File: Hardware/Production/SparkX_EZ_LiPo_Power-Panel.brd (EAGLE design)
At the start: 187.2 x 136.7 mm, 1656 parts, among them J10 AVR_SPI_PROG_3X2TESTPOINTS, J12 AVR_SPI_PROG_3X2TESTPOINTS, J14 AVR_SPI_PROG_3X2TESTPOINTS, J16 AVR_SPI_PROG_3X2TESTPOINTS, J18 AVR_SPI_PROG_3X2TESTPOINTS, J20 AVR_SPI_PROG_3X2TESTPOINTS, J22 AVR_SPI_PROG_3X2TESTPOINTS, J24 AVR_SPI_PROG_3X2TESTPOINTS, J26 AVR_SPI_PROG_3X2TESTPOINTS, J28 AVR_SPI_PROG_3X2TESTPOINTS, J3 AVR_SPI_PROG_3X2TESTPOINTS, J30 AVR_SPI_PROG_3X2TESTPOINTS, J32 AVR_SPI_PROG_3X2TESTPOINTS, J34 AVR_SPI_PROG_3X2TESTPOINTS, J36 AVR_SPI_PROG_3X2TESTPOINTS, J38 AVR_SPI_PROG_3X2TESTPOINTS, J4 AVR_SPI_PROG_3X2TESTPOINTS, J40 AVR_SPI_PROG_3X2TESTPOINTS, J42 AVR_SPI_PROG_3X2TESTPOINTS, J44 AVR_SPI_PROG_3X2TESTPOINTS, J46 AVR_SPI_PROG_3X2TESTPOINTS, J48 AVR_SPI_PROG_3X2TESTPOINTS, J50 AVR_SPI_PROG_3X2TESTPOINTS, J52 AVR_SPI_PROG_3X2TESTPOINTS, J54 AVR_SPI_PROG_3X2TESTPOINTS, J56 AVR_SPI_PROG_3X2TESTPOINTS, J58 AVR_SPI_PROG_3X2TESTPOINTS, J6 AVR_SPI_PROG_3X2TESTPOINTS, J60 AVR_SPI_PROG_3X2TESTPOINTS, J8 AVR_SPI_PROG_3X2TESTPOINTS, Q1 3.1A/30V/105mΩ, Q10 3.1A/30V/105mΩ, Q11 3.1A/30V/105mΩ, Q12 3.1A/30V/105mΩ, Q13 3.1A/30V/105mΩ, Q14 3.1A/30V/105mΩ, Q15 3.1A/30V/105mΩ, Q16 3.1A/30V/105mΩ, Q17 3.1A/30V/105mΩ, Q18 3.1A/30V/105mΩ, Q19 3.1A/30V/105mΩ, Q2 3.1A/30V/105mΩ, Q20 3.1A/30V/105mΩ, Q21 3.1A/30V/105mΩ, Q22 3.1A/30V/105mΩ, Q23 3.1A/30V/105mΩ, Q24 3.1A/30V/105mΩ, Q25 3.1A/30V/105mΩ, Q26 3.1A/30V/105mΩ, Q27 3.1A/30V/105mΩ, Q28 3.1A/30V/105mΩ, Q29 3.1A/30V/105mΩ, Q3 3.1A/30V/105mΩ, Q30 3.1A/30V/105mΩ, Q4 3.1A/30V/105mΩ, Q5 3.1A/30V/105mΩ, Q6 3.1A/30V/105mΩ, Q7 3.1A/30V/105mΩ, Q8 3.1A/30V/105mΩ, Q9 3.1A/30V/105mΩ, U1 STLQ015-3.3V, U10 STLQ015-3.3V, U100 STLQ015-3.3V, U101 MCP73831, U102 3.3V, U103 MAX17048, U104 ATTINY841-ARDUINO_QFN20M1, U105 STLQ015-3.3V, U106 MCP73831, U107 3.3V, U108 MAX17048, U109 ATTINY841-ARDUINO_QFN20M1, U11 MCP73831, U110 STLQ015-3.3V, U111 MCP73831, U112 3.3V, U113 MAX17048, U114 ATTINY841-ARDUINO_QFN20M1, U115 STLQ015-3.3V, U116 MCP73831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

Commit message: Final tweaks
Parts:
- added U$481, U$482, U$498, U$499: (no value), output:EZ_POWER_LIPO0
- added U$483, U$500: (no value), output:#BATT##0
- added U$484, U$501: (no value), output:#VIN#0
- added U$485, U$502: (no value), output:#3V3_EN#0
- added U$486, U$503: (no value), output:#PROC_PWR#0
- added U$487, U$504: (no value), output:#AT_VCC#0
- added U$488, U$505: (no value), output:#FG_SDA#0
- added U$489, U$506: (no value), output:CHG0
- added U$490, U$507: (no value), output:#RXD0#0
- added U$491, U$508: (no value), output:#TXD0#0
- added U$492, U$509: (no value), output:5#5V0
- added U$493, U$510: (no value), output:MAX0
- added U$494, U$496: SPARKX-LOGO3, SparkX:SPARKX-SMALL
- added U$495: (no value), output:#OUT#0
- added U$497: (no value), output:#IN#0
- U$100, U$372: device output:#IN#0 -> output:#TXD0#0
- U$101, U$118, U$373, U$390: device output:EZ_POWER_LIPO0 -> output:5#5V0
- U$102, U$357, U$374, U$85: device output:EZ_POWER_LIPO0 -> output:MAX0
- U$103, U$343, U$375, U$71: value (none) -> SPARKX-LOGO3; device output:#BATT##0 -> SparkX:SPARKX-SMALL
- U$104, U$376: device output:#VIN#0 -> output:#OUT#0
- U$105, U$137, U$377, U$409: value (none) -> SPARKX-LOGO3; device output:#3V3_EN#0 -> SparkX:SPARKX-SMALL
- U$106, U$378: device output:#PROC_PWR#0 -> output:#IN#0
- U$107, U$363, U$379, U$91: device output:#AT_VCC#0 -> output:EZ_POWER_LIPO0
- U$108, U$124, U$380, U$396: device output:#FG_SDA#0 -> output:EZ_POWER_LIPO0
- U$109, U$381: device output:CHG0 -> output:#BATT##0
- U$11, U$238: device output:5#5V_MAX0 -> output:MAX0
- U$110, U$382: device output:5#5V_MAX0 -> output:#VIN#0
- U$111, U$383: device output:#RXD0#0 -> output:#3V3_EN#0
- U$112, U$384: device output:#TXD0#0 -> output:#PROC_PWR#0
- U$113, U$147, U$385, U$419: value SPARKX-LOGO3 -> (none); device SparkX:SPARKX-SMALL -> output:#AT_VCC#0
- U$114, U$386: device output:#OUT#0 -> output:#FG_SDA#0
- U$115, U$353, U$387, U$81: value SPARKX-LOGO3 -> (none); device SparkX:SPARKX-SMALL -> output:CHG0
- U$116, U$388: device output:#IN#0 -> output:#RXD0#0
- U$117, U$134, U$389, U$406: device output:EZ_POWER_LIPO0 -> output:#TXD0#0
- U$119, U$391: device output:#BATT##0 -> output:MAX0
- U$120, U$360, U$392, U$88: value (none) -> SPARKX-LOGO3; device output:#VIN#0 -> SparkX:SPARKX-SMALL
- U$121, U$393: device output:#3V3_EN#0 -> output:#OUT#0
- U$122, U$154, U$394, U$426: value (none) -> SPARKX-LOGO3; device output:#PROC_PWR#0 -> SparkX:SPARKX-SMALL
- U$123, U$395: device output:#AT_VCC#0 -> output:#IN#0
- U$125, U$141, U$397, U$413: device output:CHG0 -> output:EZ_POWER_LIPO0
- U$126, U$398: device output:5#5V_MAX0 -> output:#BATT##0
- U$127, U$399: device output:#RXD0#0 -> output:#VIN#0
- U$128, U$400: device output:#TXD0#0 -> output:#3V3_EN#0
- U$129, U$163, U$401, U$435: value SPARKX-LOGO3 -> (none); device SparkX:SPARKX-SMALL -> output:#PROC_PWR#0
- U$130, U$402: device output:#OUT#0 -> output:#AT_VCC#0
- U$131, U$369, U$403, U$97: value SPARKX-LOGO3 -> (none); device SparkX:SPARKX-SMALL -> output:#FG_SDA#0
- U$132, U$404: device output:#IN#0 -> output:CHG0
- U$133, U$150, U$405, U$422: device output:EZ_POWER_LIPO0 -> output:#RXD0#0
- U$135, U$407: device output:#BATT##0 -> output:5#5V0
- U$136, U$408: device output:#VIN#0 -> output:MAX0
- U$138, U$410: device output:#PROC_PWR#0 -> output:#OUT#0
- U$139, U$171, U$411, U$443: value (none) -> SPARKX-LOGO3; device output:#AT_VCC#0 -> SparkX:SPARKX-SMALL
- U$140, U$412: device output:#FG_SDA#0 -> output:#IN#0
- U$142, U$158, U$414, U$430: device output:5#5V_MAX0 -> output:EZ_POWER_LIPO0
- U$143, U$415: device output:#RXD0#0 -> output:#BATT##0
- U$144, U$416: device output:#TXD0#0 -> output:#VIN#0
- U$145, U$179, U$417, U$451: value SPARKX-LOGO3 -> (none); device SparkX:SPARKX-SMALL -> output:#3V3_EN#0
- U$146, U$418: device output:#OUT#0 -> output:#PROC_PWR#0
- U$148, U$420: device output:#IN#0 -> output:#FG_SDA#0
- U$149, U$166, U$421, U$438: device output:EZ_POWER_LIPO0 -> output:CHG0
- U$151, U$423: device output:#BATT##0 -> output:#TXD0#0
- U$152, U$424: device output:#VIN#0 -> output:5#5V0
- U$153, U$425: device output:#3V3_EN#0 -> output:MAX0
- U$155, U$427: device output:#AT_VCC#0 -> output:#OUT#0
- U$156, U$188, U$428, U$460: value (none) -> SPARKX-LOGO3; device output:#FG_SDA#0 -> SparkX:SPARKX-SMALL
- U$157, U$429: device output:CHG0 -> output:#IN#0
- U$159, U$175, U$431, U$447: device output:#RXD0#0 -> output:EZ_POWER_LIPO0
- U$16, U$305, U$33, U$339, U$67: value SPARKX-LOGO3 -> (none); device SparkX:SPARKX-SMALL -> output:5#5V0
- U$160, U$432: device output:#TXD0#0 -> output:#BATT##0
- U$161, U$195, U$433, U$467: value SPARKX-LOGO3 -> (none); device SparkX:SPARKX-SMALL -> output:#VIN#0
- U$162, U$434: device output:#OUT#0 -> output:#3V3_EN#0
- U$164, U$436: device output:#IN#0 -> output:#AT_VCC#0
- U$165, U$182, U$437, U$454: device output:EZ_POWER_LIPO0 -> output:#FG_SDA#0
- U$167, U$439: device output:#BATT##0 -> output:#RXD0#0
- U$168, U$440: device output:#VIN#0 -> output:#TXD0#0
- U$169, U$441: device output:#3V3_EN#0 -> output:5#5V0
- U$17, U$258, U$290: value (none) -> SPARKX-LOGO3; device output:#OUT#0 -> SparkX:SPARKX-SMALL
- U$170, U$442: device output:#PROC_PWR#0 -> output:MAX0
- U$172, U$444: device output:#FG_SDA#0 -> output:#OUT#0
- U$173, U$205, U$445, U$477: value (none) -> SPARKX-LOGO3; device output:CHG0 -> SparkX:SPARKX-SMALL
- U$174, U$446: device output:5#5V_MAX0 -> output:#IN#0
- U$176, U$192, U$448, U$464: device output:#TXD0#0 -> output:EZ_POWER_LIPO0
- U$177, U$211, U$449: value SPARKX-LOGO3 -> (none); device SparkX:SPARKX-SMALL -> output:#BATT##0
- U$178, U$450: device output:#OUT#0 -> output:#VIN#0
- U$18, U$257, U$291: value SPARKX-LOGO3 -> (none); device SparkX:SPARKX-SMALL -> output:#OUT#0
- U$180, U$452: device output:#IN#0 -> output:#PROC_PWR#0
- U$181, U$198, U$453, U$470: device output:EZ_POWER_LIPO0 -> output:#AT_VCC#0
- U$183, U$455: device output:#BATT##0 -> output:CHG0
- U$184, U$456: device output:#VIN#0 -> output:#RXD0#0
- U$185, U$457: device output:#3V3_EN#0 -> output:#TXD0#0
- U$186, U$458: device output:#PROC_PWR#0 -> output:5#5V0
- U$187, U$459: device output:#AT_VCC#0 -> output:MAX0
- U$189, U$461: device output:CHG0 -> output:#OUT#0
- U$19, U$292, U$324, U$52: value (none) -> SPARKX-LOGO3; device output:#IN#0 -> SparkX:SPARKX-SMALL
- U$190, U$222, U$462: value (none) -> SPARKX-LOGO3; device output:5#5V_MAX0 -> SparkX:SPARKX-SMALL
- U$191, U$463: device output:#RXD0#0 -> output:#IN#0
- U$193, U$209, U$227, U$243, U$465: value SPARKX-LOGO3 -> (none); device SparkX:SPARKX-SMALL -> output:EZ_POWER_LIPO0
- U$194, U$466: device output:#OUT#0 -> output:#BATT##0
- U$196, U$468: device output:#IN#0 -> output:#3V3_EN#0
- U$197, U$214, U$469: device output:EZ_POWER_LIPO0 -> output:#PROC_PWR#0
- U$199, U$471: device output:#BATT##0 -> output:#FG_SDA#0
- U$200, U$472: device output:#VIN#0 -> output:CHG0
- U$201, U$473: device output:#3V3_EN#0 -> output:#RXD0#0
- U$202, U$474: device output:#PROC_PWR#0 -> output:#TXD0#0
- U$203, U$475: device output:#AT_VCC#0 -> output:5#5V0
- U$204, U$476: device output:#FG_SDA#0 -> output:MAX0
- U$206, U$478: device output:5#5V_MAX0 -> output:#OUT#0
- U$207, U$239, U$479: value (none) -> SPARKX-LOGO3; device output:#RXD0#0 -> SparkX:SPARKX-SMALL
- U$208, U$480: device output:#TXD0#0 -> output:#IN#0
- U$21, U$293, U$310, U$38: device output:EZ_POWER_LIPO0 -> output:#IN#0
- U$210, U$226: device output:#OUT#0 -> output:EZ_POWER_LIPO0
- U$212: device output:#IN#0 -> output:#VIN#0
- U$213, U$230: device output:EZ_POWER_LIPO0 -> output:#3V3_EN#0
- U$215: device output:#BATT##0 -> output:#AT_VCC#0
- U$216: device output:#VIN#0 -> output:#FG_SDA#0
- U$217: device output:#3V3_EN#0 -> output:CHG0
- U$218: device output:#PROC_PWR#0 -> output:#RXD0#0
- U$219: device output:#AT_VCC#0 -> output:#TXD0#0
- U$220: device output:#FG_SDA#0 -> output:5#5V0
- U$221: device output:CHG0 -> output:MAX0
- U$223: device output:#RXD0#0 -> output:#OUT#0
- U$224, U$256: value (none) -> SPARKX-LOGO3; device output:#TXD0#0 -> SparkX:SPARKX-SMALL
- U$225, U$259: value SPARKX-LOGO3 -> (none); device SparkX:SPARKX-SMALL -> output:#IN#0
- U$228: device output:#IN#0 -> output:#BATT##0
- U$229, U$246: device output:EZ_POWER_LIPO0 -> output:#VIN#0
- U$23, U$295, U$311, U$39: device output:#BATT##0 -> output:EZ_POWER_LIPO0
- U$231: device output:#BATT##0 -> output:#PROC_PWR#0
- U$232: device output:#VIN#0 -> output:#AT_VCC#0
- U$233: device output:#3V3_EN#0 -> output:#FG_SDA#0
- U$234: device output:#PROC_PWR#0 -> output:CHG0
- U$235: device output:#AT_VCC#0 -> output:#RXD0#0
- U$236: device output:#FG_SDA#0 -> output:#TXD0#0
- U$237: device output:CHG0 -> output:5#5V0
- U$24, U$296: device output:#VIN#0 -> output:#BATT##0
- U$240: device output:#TXD0#0 -> output:#OUT#0
- U$242: device output:#OUT#0 -> output:#IN#0
- U$244, U$260: device output:#IN#0 -> output:EZ_POWER_LIPO0
- U$245, U$262: device output:EZ_POWER_LIPO0 -> output:#BATT##0
- U$247: device output:#BATT##0 -> output:#3V3_EN#0
- U$248: device output:#VIN#0 -> output:#PROC_PWR#0
- U$249: device output:#3V3_EN#0 -> output:#AT_VCC#0
- U$25, U$297: device output:#3V3_EN#0 -> output:#VIN#0
- U$250: device output:#PROC_PWR#0 -> output:#FG_SDA#0
- U$251: device output:#AT_VCC#0 -> output:CHG0
- U$252: device output:#FG_SDA#0 -> output:#RXD0#0
- U$253: device output:CHG0 -> output:#TXD0#0
- U$254: device output:5#5V_MAX0 -> output:5#5V0
- U$255: device output:#RXD0#0 -> output:MAX0
- U$26, U$298: device output:#PROC_PWR#0 -> output:#3V3_EN#0
- U$263: device output:#BATT##0 -> output:#VIN#0
- U$264: device output:#VIN#0 -> output:#3V3_EN#0
- U$265: device output:#3V3_EN#0 -> output:#PROC_PWR#0
- U$266: device output:#PROC_PWR#0 -> output:#AT_VCC#0
- U$267: device output:#AT_VCC#0 -> output:#FG_SDA#0
- U$268: device output:#FG_SDA#0 -> output:CHG0
- U$269: device output:CHG0 -> output:#RXD0#0
- U$27, U$299: device output:#AT_VCC#0 -> output:#PROC_PWR#0
- U$270: device output:5#5V_MAX0 -> output:#TXD0#0
- U$271: device output:#RXD0#0 -> output:5#5V0
- U$272: device output:#TXD0#0 -> output:MAX0
- U$28, U$300: device output:#FG_SDA#0 -> output:#AT_VCC#0
- U$286: device output:5#5V_MAX0 -> output:#RXD0#0
- U$287: device output:#RXD0#0 -> output:#TXD0#0
- U$288: device output:#TXD0#0 -> output:5#5V0
- U$289, U$323, U$51: value SPARKX-LOGO3 -> (none); device SparkX:SPARKX-SMALL -> output:MAX0
- U$29, U$301: device output:CHG0 -> output:#FG_SDA#0
- U$30, U$302: device output:5#5V_MAX0 -> output:CHG0
- U$306, U$34: device output:#OUT#0 -> output:MAX0
- U$308, U$36: device output:#IN#0 -> output:#OUT#0
- U$309, U$326, U$341, U$358, U$37, U$54, U$69, U$86: value (none) -> SPARKX-LOGO3; device output:EZ_POWER_LIPO0 -> SparkX:SPARKX-SMALL
- U$312, U$328, U$40, U$56: device output:#VIN#0 -> output:EZ_POWER_LIPO0
- U$313, U$41: device output:#3V3_EN#0 -> output:#BATT##0
- U$314, U$42: device output:#PROC_PWR#0 -> output:#VIN#0
- U$315, U$43: device output:#AT_VCC#0 -> output:#3V3_EN#0
- U$316, U$44: device output:#FG_SDA#0 -> output:#PROC_PWR#0
- U$317, U$45: device output:CHG0 -> output:#AT_VCC#0
- U$318, U$46: device output:5#5V_MAX0 -> output:#FG_SDA#0
- U$319, U$47: device output:#RXD0#0 -> output:CHG0
- U$320, U$48: device output:#TXD0#0 -> output:#RXD0#0
- U$321, U$355, U$49, U$83: value SPARKX-LOGO3 -> (none); device SparkX:SPARKX-SMALL -> output:#TXD0#0
- U$322, U$50: device output:#OUT#0 -> output:5#5V0
- U$325, U$342, U$53, U$70: device output:EZ_POWER_LIPO0 -> output:#OUT#0
- U$327, U$55: device output:#BATT##0 -> output:#IN#0
- U$329, U$345, U$57, U$73: device output:#3V3_EN#0 -> output:EZ_POWER_LIPO0
- U$330, U$58: device output:#PROC_PWR#0 -> output:#BATT##0
- U$331, U$59: device output:#AT_VCC#0 -> output:#VIN#0
- U$332, U$60: device output:#FG_SDA#0 -> output:#3V3_EN#0
- U$333, U$61: device output:CHG0 -> output:#PROC_PWR#0
- U$334, U$62: device output:5#5V_MAX0 -> output:#AT_VCC#0
- U$335, U$63: device output:#RXD0#0 -> output:#FG_SDA#0
- U$336, U$64: device output:#TXD0#0 -> output:CHG0
- U$337, U$371, U$65, U$99: value SPARKX-LOGO3 -> (none); device SparkX:SPARKX-SMALL -> output:#RXD0#0
- U$338, U$66: device output:#OUT#0 -> output:#TXD0#0
- U$340, U$68: device output:#IN#0 -> output:MAX0
- U$344, U$72: device output:#VIN#0 -> output:#IN#0
- U$346, U$362, U$74, U$90: device output:#PROC_PWR#0 -> output:EZ_POWER_LIPO0
- U$347, U$75: device output:#AT_VCC#0 -> output:#BATT##0
- U$348, U$76: device output:#FG_SDA#0 -> output:#VIN#0
- U$349, U$77: device output:CHG0 -> output:#3V3_EN#0
- U$350, U$78: device output:5#5V_MAX0 -> output:#PROC_PWR#0
- U$351, U$79: device output:#RXD0#0 -> output:#AT_VCC#0
- U$352, U$80: device output:#TXD0#0 -> output:#FG_SDA#0
- U$354, U$82: device output:#OUT#0 -> output:#RXD0#0
- U$356, U$84: device output:#IN#0 -> output:5#5V0
- U$359, U$87: device output:#BATT##0 -> output:#OUT#0
- U$361, U$89: device output:#3V3_EN#0 -> output:#IN#0
- U$364, U$92: device output:#FG_SDA#0 -> output:#BATT##0
- U$365, U$93: device output:CHG0 -> output:#VIN#0
- U$366, U$94: device output:5#5V_MAX0 -> output:#3V3_EN#0
- U$367, U$95: device output:#RXD0#0 -> output:#PROC_PWR#0
- U$368, U$96: device output:#TXD0#0 -> output:#AT_VCC#0
- U$370, U$98: device output:#OUT#0 -> output:CHG0
- moved U$164 164.7 mm to (155.6, 8.64), flipped to the top, turned to 90 degrees
- moved U$333 163.2 mm to (150.7, 44.9), flipped to the bottom, turned to 0 degrees
- moved U$168 160.8 mm to (154.4, 16.5)
- moved U$334 160.2 mm to (155.6, 49.8)
- moved U$328 159.4 mm to (156.1, 67.2), flipped to the top, turned to 90 degrees
- moved U$163 158.4 mm to (150.7, 3.75)
- moved U$335 157.2 mm to (156.1, 69.8)
- moved U$332 156.4 mm to (153.3, 48.8), turned to 0 degrees
- moved U$324 155.8 mm to (147.8, 54.0), flipped to the top, turned to 90 degrees
- moved U$167 155.7 mm to (147.9, 16.5), turned to 90 degrees
- moved U$325 155.2 mm to (151.6, 46.0), turned to 0 degrees
- moved U$327 153.5 mm to (151.6, 75.9)
- moved U$162 152.9 mm to (153.3, 7.62), flipped to the bottom
- moved U$170 151.7 mm to (155.5, 31.0), flipped to the top
- moved U$165 151.5 mm to (156.1, 28.7), flipped to the bottom
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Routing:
- net GND1: track 82.0 -> 96.0 mm
- net GND7: track 82.0 -> 96.0 mm
- net GND6: track 82.0 -> 96.0 mm
- net GND5: track 82.0 -> 96.0 mm
- net GND2: track 82.0 -> 96.0 mm
- net GND3: track 82.0 -> 96.0 mm
- net GND9: track 82.0 -> 96.0 mm
- net GND8: track 82.0 -> 96.0 mm
- net GND4: track 82.0 -> 96.0 mm
- net GND19: track 82.0 -> 96.0 mm
- net GND18: track 82.0 -> 96.0 mm
- net GND: track 82.0 -> 96.0 mm
- net GND29: track 82.0 -> 96.0 mm
- net GND28: track 82.0 -> 96.0 mm
- net GND27: track 82.0 -> 96.0 mm
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
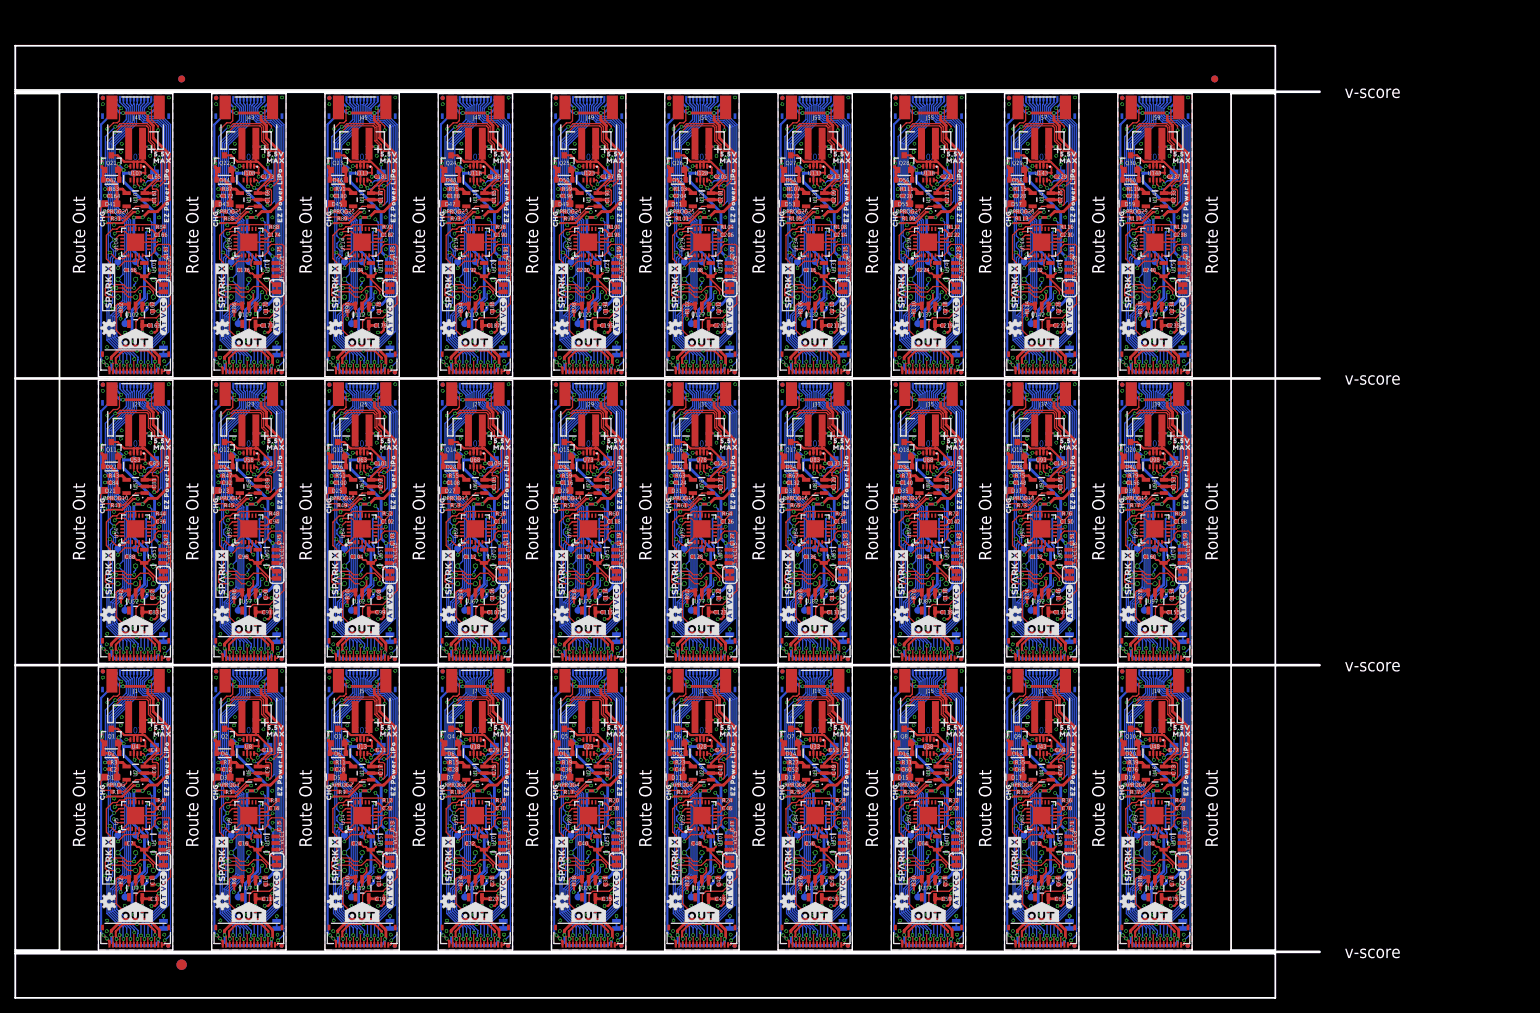
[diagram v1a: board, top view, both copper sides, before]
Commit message: Gapless production panel
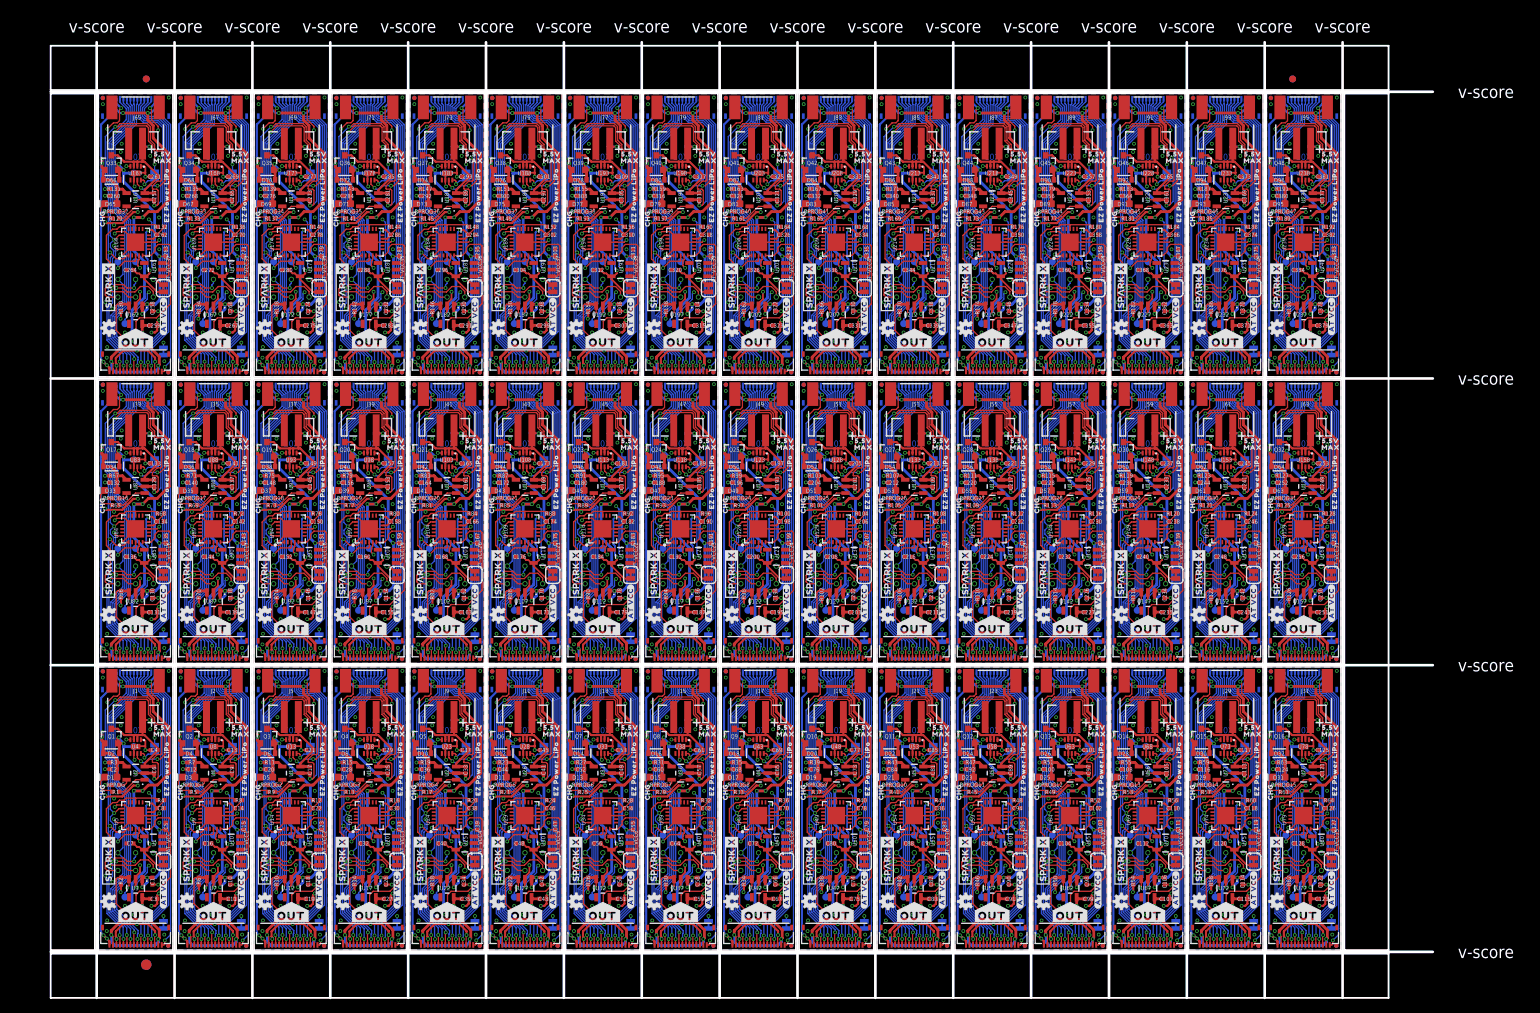
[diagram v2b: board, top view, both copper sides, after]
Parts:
- added 3V3_EN30, 3V3_EN31, 3V3_EN32, 3V3_EN33, 3V3_EN34, 3V3_EN35, 3V3_EN36, 3V3_EN37, 3V3_EN38, 3V3_EN39, 3V3_EN40, 3V3_EN41, 3V3_EN42, 3V3_EN43, 3V3_EN44, 3V3_EN45, 3V3_EN46, 3V3_EN47, BATT+30, BATT+31, BATT+32, BATT+33, BATT+34, BATT+35, BATT+36, BATT+37, BATT+38, BATT+39, BATT+40, BATT+41, BATT+42, BATT+43, BATT+44, BATT+45, BATT+46, BATT+47, RXD30, RXD31, RXD32, RXD33, RXD34, RXD35, RXD36, RXD37, RXD38, RXD39, RXD40, RXD41, RXD42, RXD43, RXD44, RXD45, RXD46, RXD47, TXD30, TXD31, TXD32, TXD33, TXD34, TXD35, TXD36, TXD37, TXD38, TXD39, TXD40, TXD41, TXD42, TXD43, TXD44, TXD45, TXD46, TXD47, VIN30, VIN31, VIN32, VIN33, VIN34, VIN35, VIN36, VIN37, VIN38, VIN39, VIN40, VIN41, VIN42, VIN43, VIN44, VIN45, VIN46, VIN47: TEST-POINT3X4, SparkFun-Connectors:PAD.03X.04
- added AT_VCC30, AT_VCC31, AT_VCC32, AT_VCC33, AT_VCC34, AT_VCC35, AT_VCC36, AT_VCC37, AT_VCC38, AT_VCC39, AT_VCC40, AT_VCC41, AT_VCC42, AT_VCC43, AT_VCC44, AT_VCC45, AT_VCC46, AT_VCC47, FG_SDA30, FG_SDA31, FG_SDA32, FG_SDA33, FG_SDA34, FG_SDA35, FG_SDA36, FG_SDA37, FG_SDA38, FG_SDA39, FG_SDA40, FG_SDA41, FG_SDA42, FG_SDA43, FG_SDA44, FG_SDA45, FG_SDA46, FG_SDA47, PROC_PWR_EN30, PROC_PWR_EN31, PROC_PWR_EN32, PROC_PWR_EN33, PROC_PWR_EN34, PROC_PWR_EN35, PROC_PWR_EN36, PROC_PWR_EN37, PROC_PWR_EN38, PROC_PWR_EN39, PROC_PWR_EN40, PROC_PWR_EN41, PROC_PWR_EN42, PROC_PWR_EN43, PROC_PWR_EN44, PROC_PWR_EN45, PROC_PWR_EN46, PROC_PWR_EN47: JUMPER-SMT_2_NC_TRACE_SILK, SparkFun-Jumpers:SMT-JUMPER_2_NC_TRACE_SILK
- added C241, C249, C257, C265, C273, C281, C289, C297, C305, C313, C321, C329, C337, C345, C353, C361, C369, C377: 4.7uF, SparkFun-Capacitors:0402-TIGHT
- added C242, C243, C244, C247, C248, C250, C251, C252, C255, C256, C258, C259, C260, C263, C264, C266, C267, C268, C271, C272, C274, C275, C276, C279, C280, C282, C283, C284, C287, C288, C290, C291, C292, C295, C296, C298, C299, C300, C303, C304, C306, C307, C308, C311, C312, C314, C315, C316, C319, C320, C322, C323, C324, C327, C328, C330, C331, C332, C335, C336, C338, C339, C340, C343, C344, C346, C347, C348, C351, C352, C354, C355, C356, C359, C360, C362, C363, C364, C367, C368, C370, C371, C372, C375, C376, C378, C379, C380, C383, C384: 2.2uF, SparkFun-Capacitors:0402-TIGHT
- added C245, C246, C253, C254, C261, C262, C269, C270, C277, C278, C285, C286, C293, C294, C301, C302, C309, C310, C317, C318, C325, C326, C333, C334, C341, C342, C349, C350, C357, C358, C365, C366, C373, C374, C381, C382: 0.1uF, SparkFun-Capacitors:0402-TIGHT
- added D61, D63, D65, D67, D69, D71, D73, D75, D77, D79, D81, D83, D85, D87, D89, D91, D93, D95: Yellow, SparkFun-LED:LED-0603
- added D62, D64, D66, D68, D70, D72, D74, D76, D78, D80, D82, D84, D86, D88, D90, D92, D94, D96: 1A/23V/620mV, SparkFun-DiscreteSemi:SOD-323
- added FD121, FD122, FD123, FD124, FD125, FD126, FD127, FD128, FD129, FD130, FD131, FD132, FD133, FD134, FD135, FD136, FD137, FD138, FD139, FD140, FD141, FD142, FD143, FD144, FD145, FD146, FD147, FD148, FD149, FD150, FD151, FD152, FD153, FD154, FD155, FD156, FD157, FD158, FD159, FD160, FD161, FD162, FD163, FD164, FD165, FD166, FD167, FD168, FD169, FD170, FD171, FD172, FD173, FD174, FD175, FD176, FD177, FD178, FD179, FD180, FD181, FD182, FD183, FD184, FD185, FD186, FD187, FD188, FD189, FD190, FD191, FD192: FIDUCIALUFIDUCIAL, SparkFun-Aesthetics:FIDUCIAL-MICRO
- added IN30, IN31, IN32, IN33, IN34, IN35, IN36, IN37, IN38, IN39, IN40, IN41, IN42, IN43, IN44, IN45, IN46, IN47, OUT30, OUT31, OUT32, OUT33, OUT34, OUT35, OUT36, OUT37, OUT38, OUT39, OUT40, OUT41, OUT42, OUT43, OUT44, OUT45, OUT46, OUT47: FPC_16_0.5MM_BACKFLIP, New_Parts_Connectors:FPC_16_DOUBLESIDED_BACKFLIP
- added J61, J63, J65, J67, J69, J71, J73, J75, J77, J79, J81, J83, J85, J87, J89, J91, J93, J95: (no value), SparkFun-Connectors:JST-2-SMD
- added J62, J64, J66, J68, J70, J72, J74, J76, J78, J80, J82, J84, J86, J88, J90, J92, J94, J96: AVR_SPI_PROG_3X2TESTPOINTS, SparkFun-Connectors:2X3_TEST_POINTS
- added LOGO61, LOGO62, LOGO63, LOGO64, LOGO65, LOGO66, LOGO67, LOGO68, LOGO69, LOGO70, LOGO71, LOGO72, LOGO73, LOGO74, LOGO75, LOGO76, LOGO77, LOGO78, LOGO79, LOGO80, LOGO81, LOGO82, LOGO83, LOGO84, LOGO85, LOGO86, LOGO87, LOGO88, LOGO89, LOGO90, LOGO91, LOGO92, LOGO93, LOGO94, LOGO95, LOGO96: OSHW-LOGOMINI, SparkFun-Aesthetics:OSHW-LOGO-MINI
- added Q31, Q32, Q33, Q34, Q35, Q36, Q37, Q38, Q39, Q40, Q41, Q42, Q43, Q44, Q45, Q46, Q47, Q48: 3.1A/30V/105mΩ, SparkFun-DiscreteSemi:SOT23-3
- added R121, R125, R129, R133, R137, R141, R145, R149, R153, R157, R161, R165, R169, R173, R177, R181, R185, R189: 1k, SparkFun-Resistors:0402-TIGHT
- added R122, R123, R126, R127, R130, R131, R134, R135, R138, R139, R142, R143, R146, R147, R150, R151, R154, R155, R158, R159, R162, R163, R166, R167, R170, R171, R174, R175, R178, R179, R182, R183, R186, R187, R190, R191: 100k, SparkFun-Resistors:0402-TIGHT
- added R124, R128, R132, R136, R140, R144, R148, R152, R156, R160, R164, R168, R172, R176, R180, R184, R188, R192: 4.7k, SparkFun-Resistors:0402-TIGHT
- added RPROG30, RPROG31, RPROG32, RPROG33, RPROG34, RPROG35, RPROG36, RPROG37, RPROG38, RPROG39, RPROG40, RPROG41, RPROG42, RPROG43, RPROG44, RPROG45, RPROG46, RPROG47: 10k, SparkFun-Resistors:0402-TIGHT
- added U$511, U$513, U$528, U$530, U$545, U$547, U$562, U$564, U$579, U$581, U$596, U$598, U$613, U$615, U$630, U$632, U$647, U$649, U$664, U$666, U$681, U$683, U$698, U$700, U$715, U$717, U$732, U$734, U$749, U$751, U$766, U$768, U$783, U$785, U$800, U$802: SPARKX-LOGO3, SparkX:SPARKX-SMALL
- added U$512, U$529, U$546, U$563, U$580, U$597, U$614, U$631, U$648, U$665, U$682, U$699, U$716, U$733, U$750, U$767, U$784, U$801: (no value), output:#OUT#0
- added U$514, U$531, U$548, U$565, U$582, U$599, U$616, U$633, U$650, U$667, U$684, U$701, U$718, U$735, U$752, U$769, U$786, U$803: (no value), output:#IN#0
- added U$515, U$516, U$532, U$533, U$549, U$550, U$566, U$567, U$583, U$584, U$600, U$601, U$617, U$618, U$634, U$635, U$651, U$652, U$668, U$669, U$685, U$686, U$702, U$703, U$719, U$720, U$736, U$737, U$753, U$754, U$770, U$771, U$787, U$788, U$804, U$805: (no value), output:EZ_POWER_LIPO0
- added U$517, U$534, U$551, U$568, U$585, U$602, U$619, U$636, U$653, U$670, U$687, U$704, U$721, U$738, U$755, U$772, U$789, U$806: (no value), output:#BATT##0
- added U$518, U$535, U$552, U$569, U$586, U$603, U$620, U$637, U$654, U$671, U$688, U$705, U$722, U$739, U$756, U$773, U$790, U$807: (no value), output:#VIN#0
- added U$519, U$536, U$553, U$570, U$587, U$604, U$621, U$638, U$655, U$672, U$689, U$706, U$723, U$740, U$757, U$774, U$791, U$808: (no value), output:#3V3_EN#0
- added U$520, U$537, U$554, U$571, U$588, U$605, U$622, U$639, U$656, U$673, U$690, U$707, U$724, U$741, U$758, U$775, U$792, U$809: (no value), output:#PROC_PWR#0
- added U$521, U$538, U$555, U$572, U$589, U$606, U$623, U$640, U$657, U$674, U$691, U$708, U$725, U$742, U$759, U$776, U$793, U$810: (no value), output:#AT_VCC#0
- added U$522, U$539, U$556, U$573, U$590, U$607, U$624, U$641, U$658, U$675, U$692, U$709, U$726, U$743, U$760, U$777, U$794, U$811: (no value), output:#FG_SDA#0
- added U$523, U$540, U$557, U$574, U$591, U$608, U$625, U$642, U$659, U$676, U$693, U$710, U$727, U$744, U$761, U$778, U$795, U$812: (no value), output:CHG0
- added U$524, U$541, U$558, U$575, U$592, U$609, U$626, U$643, U$660, U$677, U$694, U$711, U$728, U$745, U$762, U$779, U$796, U$813: (no value), output:#RXD0#0
- added U$525, U$542, U$559, U$576, U$593, U$610, U$627, U$644, U$661, U$678, U$695, U$712, U$729, U$746, U$763, U$780, U$797, U$814: (no value), output:#TXD0#0
- added U$526, U$543, U$560, U$577, U$594, U$611, U$628, U$645, U$662, U$679, U$696, U$713, U$730, U$747, U$764, U$781, U$798, U$815: (no value), output:5#5V0
- added U$527, U$544, U$561, U$578, U$595, U$612, U$629, U$646, U$663, U$680, U$697, U$714, U$731, U$748, U$765, U$782, U$799, U$816: (no value), output:MAX0
- added U151, U156, U161, U166, U171, U176, U181, U186, U191, U196, U201, U206, U211, U216, U221, U226, U231, U236: MCP73831, SparkFun-IC-Power:SOT23-5
- added U152, U157, U162, U167, U172, U177, U182, U187, U192, U197, U202, U207, U212, U217, U222, U227, U232, U237: 3.3V, SparkFun-IC-Power:SOT23-5
- added U153, U158, U163, U168, U173, U178, U183, U188, U193, U198, U203, U208, U213, U218, U223, U228, U233, U238: MAX17048, SparkFun-IC-Power:DFN-8
- added U154, U159, U164, U169, U174, U179, U184, U189, U194, U199, U204, U209, U214, U219, U224, U229, U234, U239: ATTINY841-ARDUINO_QFN20M1, SparkFun-IC-Microcontroller:QFN20_20M1
- added U155, U160, U165, U170, U175, U180, U185, U190, U195, U200, U205, U210, U215, U220, U225, U230, U235, U240: STLQ015-3.3V, SparkFun-IC-Power:SOT23-5
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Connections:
- new net !RESET!30: J62.5, R124.1, U154.13
- new net !RESET!31: J64.5, R128.1, U159.13
- new net !RESET!32: J66.5, R132.1, U164.13
- new net !RESET!33: J68.5, R136.1, U169.13
- new net !RESET!34: J70.5, R140.1, U174.13
- new net !RESET!35: J72.5, R144.1, U179.13
- new net !RESET!36: J74.5, R148.1, U184.13
- new net !RESET!37: J76.5, R152.1, U189.13
- new net !RESET!38: J78.5, R156.1, U194.13
- new net !RESET!39: J80.5, R160.1, U199.13
- new net !RESET!40: J82.5, R164.1, U204.13
- new net !RESET!41: J84.5, R168.1, U209.13
- new net !RESET!42: J86.5, R172.1, U214.13
- new net !RESET!43: J88.5, R176.1, U219.13
- new net !RESET!44: J90.5, R180.1, U224.13
- new net !RESET!45: J92.5, R184.1, U229.13
- new net !RESET!46: J94.5, R188.1, U234.13
- new net !RESET!47: J96.5, R192.1, U239.13
- new net 3.3V30: C243.1, IN30.15, IN30.2, OUT30.15, OUT30.2, U152.5
- new net 3.3V31: C251.1, IN31.15, IN31.2, OUT31.15, OUT31.2, U157.5
- new net 3.3V32: C259.1, IN32.15, IN32.2, OUT32.15, OUT32.2, U162.5
- new net 3.3V33: C267.1, IN33.15, IN33.2, OUT33.15, OUT33.2, U167.5
- new net 3.3V34: C275.1, IN34.15, IN34.2, OUT34.15, OUT34.2, U172.5
- new net 3.3V35: C283.1, IN35.15, IN35.2, OUT35.15, OUT35.2, U177.5
- new net 3.3V36: C291.1, IN36.15, IN36.2, OUT36.15, OUT36.2, U182.5
- new net 3.3V37: C299.1, IN37.15, IN37.2, OUT37.15, OUT37.2, U187.5
- new net 3.3V38: C307.1, IN38.15, IN38.2, OUT38.15, OUT38.2, U192.5
- new net 3.3V39: C315.1, IN39.15, IN39.2, OUT39.15, OUT39.2, U197.5
- new net 3.3V40: C323.1, IN40.15, IN40.2, OUT40.15, OUT40.2, U202.5
- new net 3.3V41: C331.1, IN41.15, IN41.2, OUT41.15, OUT41.2, U207.5
- new net 3.3V42: C339.1, IN42.15, IN42.2, OUT42.15, OUT42.2, U212.5
- new net 3.3V43: C347.1, IN43.15, IN43.2, OUT43.15, OUT43.2, U217.5
- new net 3.3V44: C355.1, IN44.15, IN44.2, OUT44.15, OUT44.2, U222.5
- new net 3.3V45: C363.1, IN45.15, IN45.2, OUT45.15, OUT45.2, U227.5
- new net 3.3V46: C371.1, IN46.15, IN46.2, OUT46.15, OUT46.2, U232.5
- new net 3.3V47: C379.1, IN47.15, IN47.2, OUT47.15, OUT47.2, U237.5
- new net 3V3_EN30: 3V3_EN30.1, R122.2, U152.3, U154.5
- new net 3V3_EN31: 3V3_EN31.1, R126.2, U157.3, U159.5
- new net 3V3_EN32: 3V3_EN32.1, R130.2, U162.3, U164.5
- new net 3V3_EN33: 3V3_EN33.1, R134.2, U167.3, U169.5
- new net 3V3_EN34: 3V3_EN34.1, R138.2, U172.3, U174.5
- new net 3V3_EN35: 3V3_EN35.1, R142.2, U177.3, U179.5
- new net 3V3_EN36: 3V3_EN36.1, R146.2, U182.3, U184.5
- new net 3V3_EN37: 3V3_EN37.1, R150.2, U187.3, U189.5
- new net 3V3_EN38: 3V3_EN38.1, R154.2, U192.3, U194.5
- new net 3V3_EN39: 3V3_EN39.1, R158.2, U197.3, U199.5
- new net 3V3_EN40: 3V3_EN40.1, R162.2, U202.3, U204.5
- new net 3V3_EN41: 3V3_EN41.1, R166.2, U207.3, U209.5
- new net 3V3_EN42: 3V3_EN42.1, R170.2, U212.3, U214.5
- new net 3V3_EN43: 3V3_EN43.1, R174.2, U217.3, U219.5
- new net 3V3_EN44: 3V3_EN44.1, R178.2, U222.3, U224.5
- new net 3V3_EN45: 3V3_EN45.1, R182.2, U227.3, U229.5
- new net 3V3_EN46: 3V3_EN46.1, R186.2, U232.3, U234.5
- new net 3V3_EN47: 3V3_EN47.1, R190.2, U237.3, U239.5
- new net AT_CIPO30: J62.1, U154.20
- new net AT_CIPO31: J64.1, U159.20
- new net AT_CIPO32: J66.1, U164.20
- new net AT_CIPO33: J68.1, U169.20
- new net AT_CIPO34: J70.1, U174.20
- new net AT_CIPO35: J72.1, U179.20
- new net AT_CIPO36: J74.1, U184.20
- new net AT_CIPO37: J76.1, U189.20
- new net AT_CIPO38: J78.1, U194.20
- new net AT_CIPO39: J80.1, U199.20
- new net AT_CIPO40: J82.1, U204.20
- new net AT_CIPO41: J84.1, U209.20
- new net AT_CIPO42: J86.1, U214.20
- new net AT_CIPO43: J88.1, U219.20
- new net AT_CIPO44: J90.1, U224.20
- new net AT_CIPO45: J92.1, U229.20
- new net AT_CIPO46: J94.1, U234.20
- new net AT_CIPO47: J96.1, U239.20
- new net AT_VCC30: AT_VCC30.2, C246.1, C248.1, R124.2, U154.9, U155.5
- new net AT_VCC31: AT_VCC31.2, C254.1, C256.1, R128.2, U159.9, U160.5
- new net AT_VCC32: AT_VCC32.2, C262.1, C264.1, R132.2, U164.9, U165.5
- new net AT_VCC33: AT_VCC33.2, C270.1, C272.1, R136.2, U169.9, U170.5
- new net AT_VCC34: AT_VCC34.2, C278.1, C280.1, R140.2, U174.9, U175.5
- new net AT_VCC35: AT_VCC35.2, C286.1, C288.1, R144.2, U179.9, U180.5
- new net AT_VCC36: AT_VCC36.2, C294.1, C296.1, R148.2, U184.9, U185.5
- new net AT_VCC37: AT_VCC37.2, C302.1, C304.1, R152.2, U189.9, U190.5
- new net AT_VCC38: AT_VCC38.2, C310.1, C312.1, R156.2, U194.9, U195.5
- new net AT_VCC39: AT_VCC39.2, C318.1, C320.1, R160.2, U199.9, U200.5
- new net AT_VCC40: AT_VCC40.2, C326.1, C328.1, R164.2, U204.9, U205.5
- new net AT_VCC41: AT_VCC41.2, C334.1, C336.1, R168.2, U209.9, U210.5
- new net AT_VCC42: AT_VCC42.2, C342.1, C344.1, R172.2, U214.9, U215.5
- new net AT_VCC43: AT_VCC43.2, C350.1, C352.1, R176.2, U219.9, U220.5
- new net AT_VCC44: AT_VCC44.2, C358.1, C360.1, R180.2, U224.9, U225.5
- new net AT_VCC45: AT_VCC45.2, C366.1, C368.1, R184.2, U229.9, U230.5
- new net AT_VCC46: AT_VCC46.2, C374.1, C376.1, R188.2, U234.9, U235.5
- new net AT_VCC47: AT_VCC47.2, C382.1, C384.1, R192.2, U239.9, U240.5
- new net CHG_LED30: R121.1, U151.1
- new net CHG_LED31: R125.1, U156.1
- new net CHG_LED32: R129.1, U161.1
- new net CHG_LED33: R133.1, U166.1
- new net CHG_LED34: R137.1, U171.1
- new net CHG_LED35: R141.1, U176.1
- new net CHG_LED36: R145.1, U181.1
- new net CHG_LED37: R149.1, U186.1
- new net CHG_LED38: R153.1, U191.1
- new net CHG_LED39: R157.1, U196.1
- new net CHG_LED40: R161.1, U201.1
- new net CHG_LED41: R165.1, U206.1
- new net CHG_LED42: R169.1, U211.1
- new net CHG_LED43: R173.1, U216.1
- new net CHG_LED44: R177.1, U221.1
- new net CHG_LED45: R181.1, U226.1
- new net CHG_LED46: R185.1, U231.1
- new net CHG_LED47: R189.1, U236.1
- new net CIPO30: IN30.6, OUT30.6
- new net CIPO31: IN31.6, OUT31.6
- new net CIPO32: IN32.6, OUT32.6
- new net CIPO33: IN33.6, OUT33.6
- new net CIPO34: IN34.6, OUT34.6
- new net CIPO35: IN35.6, OUT35.6
- new net CIPO36: IN36.6, OUT36.6
- new net CIPO37: IN37.6, OUT37.6
- new net CIPO38: IN38.6, OUT38.6
- new net CIPO39: IN39.6, OUT39.6
- new net CIPO40: IN40.6, OUT40.6
- new net CIPO41: IN41.6, OUT41.6
- new net CIPO42: IN42.6, OUT42.6
- new net CIPO43: IN43.6, OUT43.6
- new net CIPO44: IN44.6, OUT44.6
- new net CIPO45: IN45.6, OUT45.6
- new net CIPO46: IN46.6, OUT46.6
- new net CIPO47: IN47.6, OUT47.6
- new net COPI30: IN30.5, OUT30.5
- new net COPI31: IN31.5, OUT31.5
- new net COPI32: IN32.5, OUT32.5
- new net COPI33: IN33.5, OUT33.5
- new net COPI34: IN34.5, OUT34.5
- new net COPI35: IN35.5, OUT35.5
- new net COPI36: IN36.5, OUT36.5
- new net COPI37: IN37.5, OUT37.5
- new net COPI38: IN38.5, OUT38.5
- new net COPI39: IN39.5, OUT39.5
- new net COPI40: IN40.5, OUT40.5
- new net COPI41: IN41.5, OUT41.5
- new net COPI42: IN42.5, OUT42.5
- new net COPI43: IN43.5, OUT43.5
- new net COPI44: IN44.5, OUT44.5
- new net COPI45: IN45.5, OUT45.5
- new net COPI46: IN46.5, OUT46.5
- new net COPI47: IN47.5, OUT47.5
- new net CS100: IN33.8, OUT33.8
- new net CS101: IN33.9, OUT33.9
- new net CS102: IN34.7, OUT34.7
- new net CS103: IN34.8, OUT34.8
- new net CS104: IN34.9, OUT34.9
- new net CS105: IN35.7, OUT35.7
- new net CS106: IN35.8, OUT35.8
- new net CS107: IN35.9, OUT35.9
- new net CS108: IN36.7, OUT36.7
- new net CS109: IN36.8, OUT36.8
- new net CS110: IN36.9, OUT36.9
- new net CS111: IN37.7, OUT37.7
- new net CS112: IN37.8, OUT37.8
- new net CS113: IN37.9, OUT37.9
- new net CS114: IN38.7, OUT38.7
- new net CS115: IN38.8, OUT38.8
- new net CS116: IN38.9, OUT38.9
- new net CS117: IN39.7, OUT39.7
- new net CS118: IN39.8, OUT39.8
- new net CS119: IN39.9, OUT39.9
- new net CS120: IN40.7, OUT40.7
- new net CS121: IN40.8, OUT40.8
- new net CS122: IN40.9, OUT40.9
- new net CS123: IN41.7, OUT41.7
- new net CS124: IN41.8, OUT41.8
- new net CS125: IN41.9, OUT41.9
- new net CS126: IN42.7, OUT42.7
- new net CS127: IN42.8, OUT42.8
- new net CS128: IN42.9, OUT42.9
- new net CS129: IN43.7, OUT43.7
- new net CS130: IN43.8, OUT43.8
- new net CS131: IN43.9, OUT43.9
- new net CS132: IN44.7, OUT44.7
- new net CS133: IN44.8, OUT44.8
- new net CS134: IN44.9, OUT44.9
- new net CS135: IN45.7, OUT45.7
- new net CS136: IN45.8, OUT45.8
- new net CS137: IN45.9, OUT45.9
- new net CS138: IN46.7, OUT46.7
- new net CS139: IN46.8, OUT46.8
- new net CS140: IN46.9, OUT46.9
- new net CS141: IN47.7, OUT47.7
- new net CS142: IN47.8, OUT47.8
- new net CS143: IN47.9, OUT47.9
- new net CS90: IN30.7, OUT30.7
- new net CS91: IN30.8, OUT30.8
- new net CS92: IN30.9, OUT30.9
- new net CS93: IN31.7, OUT31.7
- new net CS94: IN31.8, OUT31.8
- new net CS95: IN31.9, OUT31.9
- new net CS96: IN32.7, OUT32.7
- new net CS97: IN32.8, OUT32.8
- new net CS98: IN32.9, OUT32.9
- new net CS99: IN33.7, OUT33.7
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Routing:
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- added copper zone on layer 1, net GND30
- added copper zone on layer 16, net GND30
- added copper zone on layer 1, net GND31
- added copper zone on layer 16, net GND31
- added copper zone on layer 1, net GND32
- added copper zone on layer 16, net GND32
- added copper zone on layer 1, net GND33
- added copper zone on layer 16, net GND33
- added copper zone on layer 1, net GND34
- added copper zone on layer 16, net GND34
- added copper zone on layer 1, net GND35
- added copper zone on layer 16, net GND35
- added copper zone on layer 1, net GND36
- added copper zone on layer 16, net GND36
- added copper zone on layer 1, net GND37
- added copper zone on layer 16, net GND37
- added copper zone on layer 1, net GND38
- added copper zone on layer 16, net GND38
- added copper zone on layer 1, net GND39
- added copper zone on layer 16, net GND39
- added copper zone on layer 1, net GND40
- added copper zone on layer 16, net GND40
- added copper zone on layer 1, net GND41
- added copper zone on layer 16, net GND41
- added copper zone on layer 1, net GND42
- added copper zone on layer 16, net GND42
- added copper zone on layer 1, net GND43
- added copper zone on layer 16, net GND43
- added copper zone on layer 1, net GND44
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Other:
- board size 187.2 x 136.7 mm -> 198.4 x 137.2 mm
- board text removed: "Route Out"
